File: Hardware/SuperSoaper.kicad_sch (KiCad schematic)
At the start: 45 parts, among them J1 Stepper, J2 Sensor, J3 UPDI, U1 TPS62933DRLR, U2 TMC2209-LA, U3 ATtiny2X2, U4 LM358DR

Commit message: minor details changed
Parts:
- removed L1: 6.8uH, symbol Device:L
- removed S1, S2: DSHP04TSGER, easyeda2kicad:SW-SMD_8P-P1.27-L7.8-W5.4, symbol easyeda2kicad:DSHP04TSGER
- added DC1: DC-005-5A-2.0-SMT, easyeda2kicad:DC-IN-TH_DC-005-5A-2.0-SMT, symbol easyeda2kicad:DC-005-5A-2.0-SMT
- added J1: DC_in, easyeda2kicad:CONN-TH_B4B-XH-A-LF-SN, symbol Connector:Conn_01x04_Pin
- added L1: 6.8uH, easyeda2kicad:IND-SMD_L4.5-W4.0_SCD0403T, symbol Device:L_Ferrite
- added SW1, SW2: A6S-4101-H, easyeda2kicad:SW-SMD_8P-L11.1-W6.2-P2.54-LS9.8, symbol easyeda2kicad:A6S-4101-H
- C1, C10, C11, C12, C14, C15, C16, C17, C2, C3, C4, C5, C6, C7, C8, C9: footprint (none) -> Capacitor_SMD:C_0603_1608Metric
- C13: footprint (none) -> Capacitor_SMD:C_Elec_8x10.2
- J2: renamed from J1; footprint (none) -> easyeda2kicad:CONN-TH_B4B-XH-A-LF-SN; symbol Connector:Conn_01x04_Pin -> Connector:Conn_01x03_Pin
- J3: renamed from J2; footprint (none) -> easyeda2kicad:HDR-TH_3P-P2.54-H-F-W10.0-N
- J4: renamed from J3; footprint (none) -> easyeda2kicad:HDR-TH_3P-P2.54-V-F
- R1, R10, R11, R12, R13, R14, R15, R16, R17, R18, R2, R3, R4, R5, R6, R7: footprint (none) -> Resistor_SMD:R_0603_1608Metric
- R8, R9: value na -> 180m 1W; footprint (none) -> Resistor_SMD:R_1206_3216Metric
- U4: footprint easyeda2kicad:SOIC-8_L5.0-W4.0-P1.27-LS6.0-BL -> Package_SO:SOIC-8_3.9x4.9mm_P1.27mm
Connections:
- net +3.3V: now also L1.2, SW1.1 (A1), SW1.2 (A2), SW1.3 (A3), SW1.4 (A4)
- net DIR: now also SW1.6 (B3)
- net GND: now also DC1.2, DC1.3, J1.2 (Pin_2), J1.4 (Pin_4), SW2.5 (B4), SW2.6 (B3), SW2.7 (B2), SW2.8 (B1)
- net MS1: now also SW1.8 (B1)
- net MS2: now also SW1.7 (B2)
- net OB2: no longer J2.4 (Pin_4)
- net SPREAD: now also SW1.5 (B4)
- net UPDI: now also SW2.1 (A1)
- net VCC: now also DC1.1, J1.1 (Pin_1), J1.3 (Pin_3)
- net at C5.2, U1.5 (SW): now also L1.1
- net at U3.4 (PA1): now also SW2.2 (A2)
- net at U3.5 (PA2): now also SW2.3 (A3)
- net at U3.7 (PA3): now also SW2.4 (A4)
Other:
- moved on the sheet: C1, C2, C3, C4, C5, C6, C7, C8, C9, R1, R17, R18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

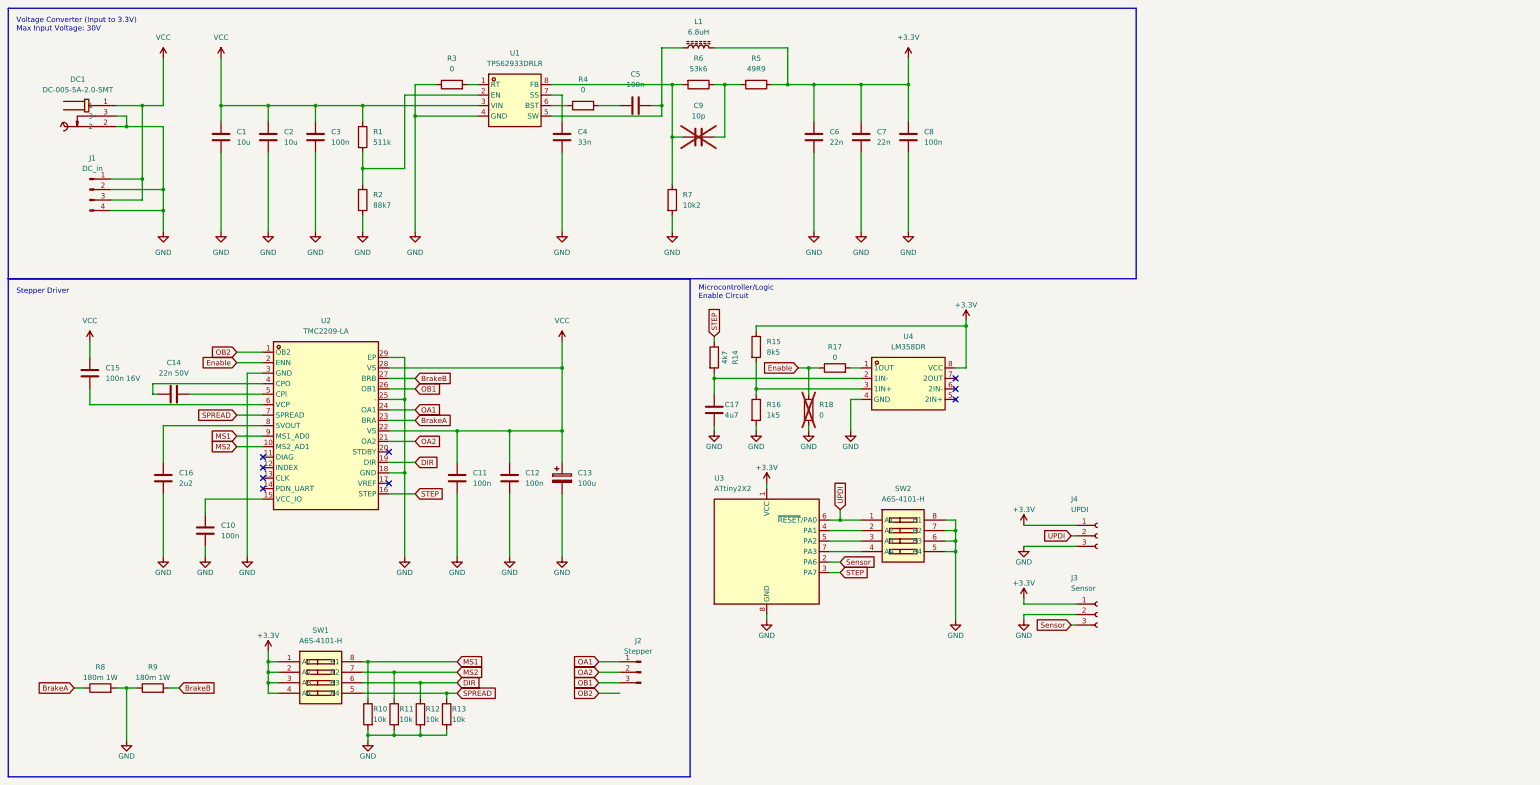
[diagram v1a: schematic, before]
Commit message: CHanged from ATtiny 2X2 to STM32C011F4P6
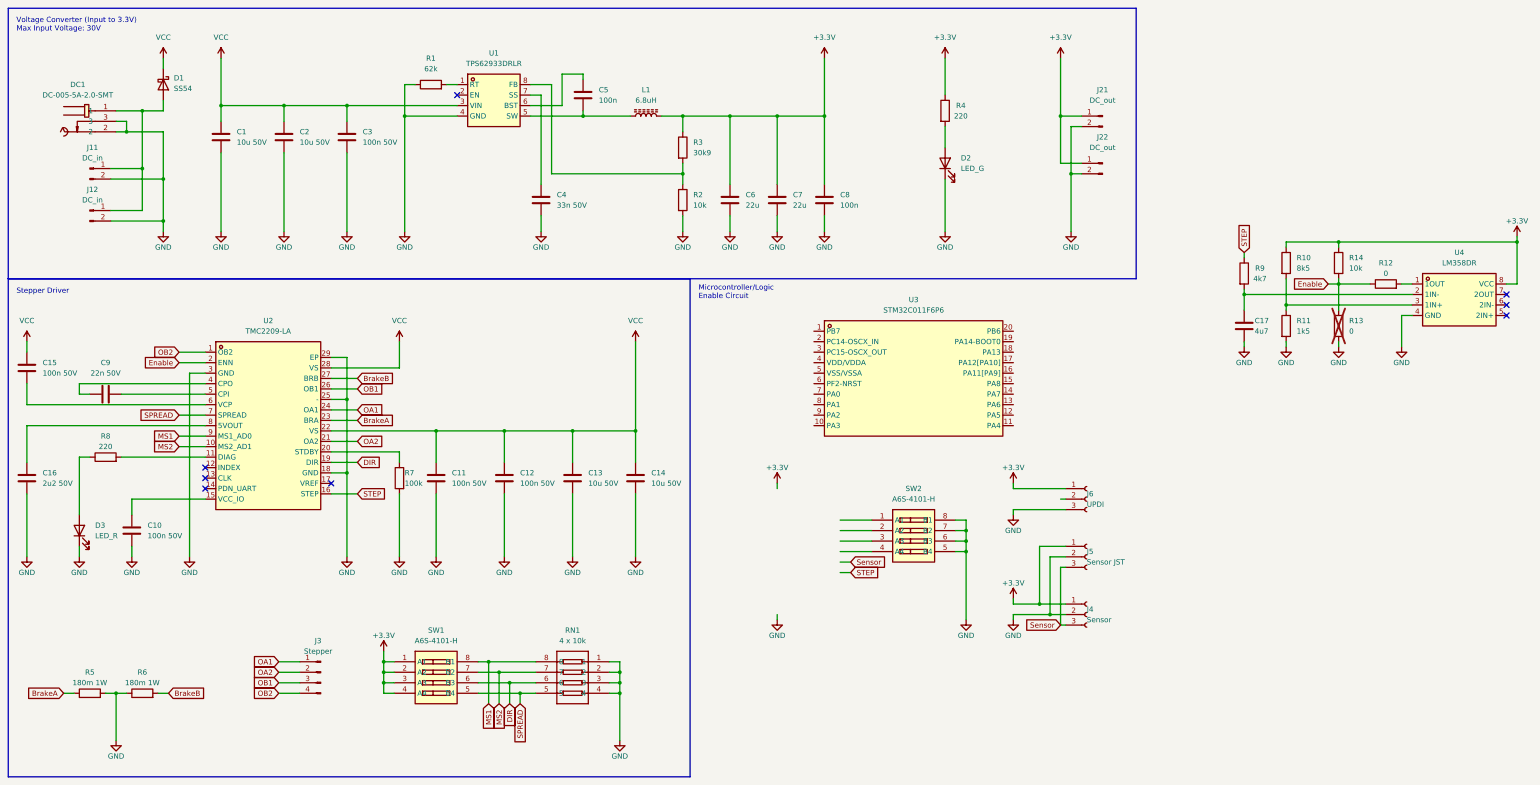
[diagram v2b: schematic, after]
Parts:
- removed C13: 100u, Capacitor_SMD:C_Elec_8x10.2, symbol Device:C_Polarized
- removed C9: 10p, Capacitor_SMD:C_0603_1608Metric, symbol Device:C
- removed J1: DC_in, easyeda2kicad:CONN-TH_B4B-XH-A-LF-SN, symbol Connector:Conn_01x04_Pin
- removed R1: 511k, Resistor_SMD:R_0603_1608Metric, symbol Device:R
- removed R10, R11, R12, R13: 10k, Resistor_SMD:R_0603_1608Metric, symbol Device:R
- removed R2: 88k7, Resistor_SMD:R_0603_1608Metric, symbol Device:R
- removed R5: 49R9, Resistor_SMD:R_0603_1608Metric, symbol Device:R
- removed U3: ATtiny2X2, Package_SO:SOIC-8_3.9x4.9mm_P1.27mm, symbol MCU_Microchip_ATtiny:ATtiny202-SS
- added C13, C14: 10u 50V, Capacitor_SMD:C_1210_3225Metric, symbol Device:C
- added D1: SS54, easyeda2kicad:SMA_L4.4-W2.8-LS5.4-R-RD, symbol Device:D_Schottky
- added D2: LED_G, LED_SMD:LED_0603_1608Metric, symbol Device:LED
- added D3: LED_R, LED_SMD:LED_0603_1608Metric, symbol Device:LED
- added J11, J12: DC_in, easyeda2kicad:CONN-TH_B2B-XH-A-LF-SN, symbol Connector:Conn_01x02_Pin
- added J21, J22: DC_out, easyeda2kicad:CONN-TH_B2B-XH-A-LF-SN, symbol Connector:Conn_01x02_Pin
- added J5: Sensor JST, easyeda2kicad:CONN-TH_S3B-XH-A-1-LF-SN, symbol Connector:Conn_01x03_Socket
- added R14: 10k, Resistor_SMD:R_0603_1608Metric, symbol Device:R
- added R7: 100k, Resistor_SMD:R_0603_1608Metric, symbol Device:R
- added R8: 220, Resistor_SMD:R_0603_1608Metric, symbol Device:R
- added RN1: 4 x 10k, easyeda2kicad:RES-ARRAY-SMD_0603-8P-L3.2-W1.6-BL, symbol easyeda2kicad:RC-ML08W103JT
- added U3: STM32C011F6P6, easyeda2kicad:TSSOP-20_L6.5-W4.4-P0.65-LS6.4-BL, symbol easyeda2kicad:STM32C011F6P6
- C1, C2: value 10u -> 10u 50V
- C10, C11, C12, C3: value 100n -> 100n 50V
- C15: value 100n 16V -> 100n 50V
- C16: value 2u2 -> 2u2 50V
- C4: value 33n -> 33n 50V
- C6, C7: value 22n -> 22u
- J3: renamed from J2; symbol Connector:Conn_01x03_Pin -> Connector:Conn_01x04_Pin
- L1: footprint easyeda2kicad:IND-SMD_L4.5-W4.0_SCD0403T -> easyeda2kicad:IND-SMD_L7.4-W7.0
- R1: renamed from R3; value 0 -> 62k
- R2: renamed from R7; value 10k2 -> 10k
- R3: renamed from R6; value 53k6 -> 30k9
- R4: value 0 -> 220
- renumbered C14 to C9, J3 to J4, J4 to J6, R15 to R10, R16 to R11, R17 to R12, R18 to R13, R8 to R5, R9 to R6, R14 to R9
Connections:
- net +3.3V: now also R3.1, R4.1, J21.1 (Pin_1), J22.1 (Pin_1), J5.1 (Pin_1), R14.1
- net DIR: now also RN1.6
- net Enable: now also R14.2
- net GND: now also C13.2, C14.2, D2.1 (K), D3.1 (K), J11.2 (Pin_2), J12.2 (Pin_2), J21.2 (Pin_2), J22.2 (Pin_2), J5.2 (Pin_2), R7.2, RN1.1, RN1.2, RN1.3, RN1.4
- net MS1: now also RN1.8
- net MS2: now also RN1.7
- net OB2: now also J3.4 (Pin_4)
- net SPREAD: now also RN1.5
- net Sensor: now also J5.3 (Pin_3)
- net VCC: now also C13.1, C14.1, D1.1 (K); no longer DC1.1
- net at U1.6 (BST): now also C5.1; no longer R4.1
- net at U2.11 (DIAG): now also R8.2
- net at U2.20 (STDBY): now also R7.1
- net at R4.2: now also D2.2 (A); no longer C5.1
- net UPDI: no longer names the net of SW2.1 (A1)
- net UPDI: no longer J6.2 (Pin_2)
- new net: D3.2 (A), R8.1
- new net: D1.2 (A), DC1.1, J11.1 (Pin_1), J12.1 (Pin_1)
- no-connect marks 9 -> 8
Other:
- moved on the sheet: C10, C11, C12, C15, C16, C17, C2, C3, C4, C5, C6, C7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

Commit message: Changed from ATtiny 2X2 to STM32C011F4P6
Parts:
- U3: value STM32C011F6P6 -> STM32C011F4P6; LCSC Part C5456198 -> C5452432
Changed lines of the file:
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@@
       (effects (font (size 1.27 1.27)))
     )
-    (property "Value" "STM32C011F6P6" (at 231.14 85.09 0)
+    (property "Value" "STM32C011F4P6" (at 231.14 85.09 0)
       (effects (font (size 1.27 1.27)))
     )
@@
       (effects (font (size 1.27 1.27)) hide)
     )
-    (property "Datasheet" "" (at 231.14 101.6 0)
+    (property "Datasheet" "https://datasheet.lcsc.com/lcsc/2305191757_STMicroelectronics-STM32C011F4P6_C5452432.pdf" (at 231.14 101.6 0)
       (effects (font (size 1.27 1.27)) hide)
     )
-    (property "LCSC Part" "C5456198" (at 231.14 123.19 0)
+    (property "LCSC Part" "C5452432" (at 231.14 123.19 0)
       (effects (font (size 1.27 1.27)) hide)
     )
